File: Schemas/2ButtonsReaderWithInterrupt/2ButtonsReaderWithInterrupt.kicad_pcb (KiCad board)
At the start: 2 copper layers, 45.7 x 36.6 mm, 17 parts, among them J1 PWR, J2 Btn out, J3 Btn in, J4 Interrupt, U1 LM393

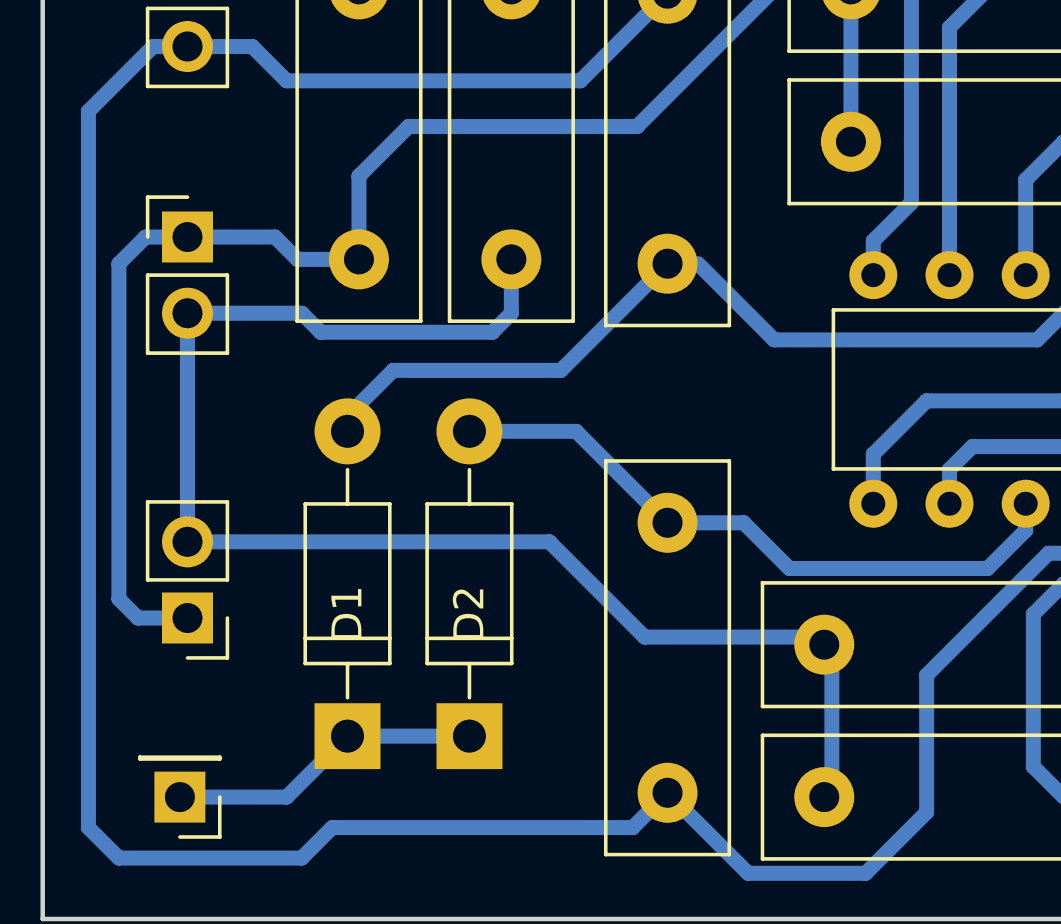
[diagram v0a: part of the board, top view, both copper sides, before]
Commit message: Add a pull down resistor
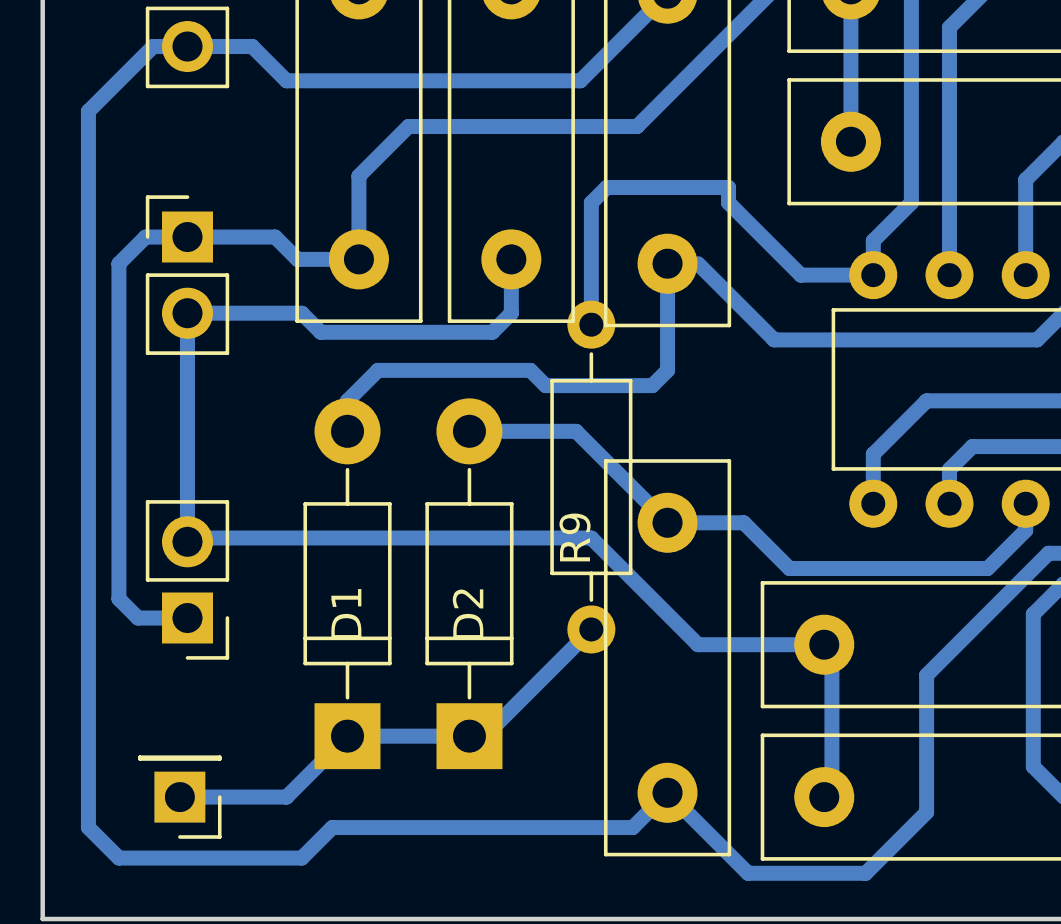
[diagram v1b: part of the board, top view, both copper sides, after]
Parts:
- added R9: R10k, Resistors_THT:R_Axial_DIN0207_L6.3mm_D2.5mm_P10.16mm_Horizontal, F.Cu at (118.9, 125.5)
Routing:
- net Net-(C2-Pad2): track 85.7 -> 100.9 mm
- net Net-(D1-Pad1): track 9.99 -> 15.5 mm
- net Net-(D1-Pad2): track 29.7 -> 33.0 mm
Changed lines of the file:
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@@
 (kicad_pcb (version 4) (host pcbnew 4.0.7-e2-6376~58~ubuntu16.04.1)
   (general
-    (links 28)
+    (links 30)
     (no_connects 0)
     (area 100.508999 108.636999 146.379001 145.363001)
     (thickness 1.6)
     (drawings 9)
-    (tracks 120)
+    (tracks 133)
     (zones 0)
-    (modules 17)
+    (modules 18)
     (nets 12)
   )
@@
     )
   )
+  (module Resistors_THT:R_Axial_DIN0207_L6.3mm_D2.5mm_P10.16mm_Horizontal (layer F.Cu)
+    (at 118.872 125.476 270)
+    (descr "Resistor, Axial_DIN0207 series, Axial, Horizontal, pin pitch=10.16mm, 0.25W = 1/4W, length*diameter=6.3*2.5mm^2, http://cdn-reichelt.de/documents/datenblatt/B400/1_4W%23YAG.pdf")
+    (tags "Resistor Axial_DIN0207 series Axial Horizontal pin pitch 10.16mm 0.25W = 1/4W length 6.3mm diameter 2.5mm")
+    (fp_text reference R9 (at 7.112 0.508 270) (layer F.SilkS)
+      (effects (font (size 1 1) (thickness 0.15)))
+    )
+    (fp_text value R10k (at 4.064 0.508 270) (layer F.Fab)
+      (effects (font (size 1 1) (thickness 0.15)))
+    )
+    (fp_line (start 1.93 -1.25) (end 1.93 1.25) (layer F.Fab) (width 0.1))
+    (fp_line (start 1.93 1.25) (end 8.23 1.25) (layer F.Fab) (width 0.1))
+    (fp_line (start 8.23 1.25) (end 8.23 -1.25) (layer F.Fab) (width 0.1))
+    (fp_line (start 8.23 -1.25) (end 1.93 -1.25) (layer F.Fab) (width 0.1))
+    (fp_line (start 0 0) (end 1.93 0) (layer F.Fab) (width 0.1))
+    (fp_line (start 10.16 0) (end 8.23 0) (layer F.Fab) (width 0.1))
+    (fp_line (start 1.87 -1.31) (end 1.87 1.31) (layer F.SilkS) (width 0.12))
+    (fp_line (start 1.87 1.31) (end 8.29 1.31) (layer F.SilkS) (width 0.12))
+    (fp_line (start 8.29 1.31) (end 8.29 -1.31) (layer F.SilkS) (width 0.12))
+    (fp_line (start 8.29 -1.31) (end 1.87 -1.31) (layer F.SilkS) (width 0.12))
+    (fp_line (start 0.98 0) (end 1.87 0) (layer F.SilkS) (width 0.12))
+    (fp_line (start 9.18 0) (end 8.29 0) (layer F.SilkS) (width 0.12))
+    (fp_line (start -1.05 -1.6) (end -1.05 1.6) (layer F.CrtYd) (width 0.05))
+    (fp_line (start -1.05 1.6) (end 11.25 1.6) (layer F.CrtYd) (width 0.05))
+    (fp_line (start 11.25 1.6) (end 11.25 -1.6) (layer F.CrtYd) (width 0.05))
+    (fp_line (start 11.25 -1.6) (end -1.05 -1.6) (layer F.CrtYd) (width 0.05))
+    (pad 1 thru_hole circle (at 0 0 270) (size 1.6 1.6) (drill 0.8) (layers *.Cu *.Mask)
+      (net 9 "Net-(C2-Pad2)"))
+    (pad 2 thru_hole oval (at 10.16 0 270) (size 1.6 1.6) (drill 0.8) (layers *.Cu *.Mask)
+      (net 3 "Net-(D1-Pad1)"))
+    (model ${KISYS3DMOD}/Resistors_THT.3dshapes/R_Axial_DIN0207_L6.3mm_D2.5mm_P10.16mm_Horizontal.wrl
+      (at (xyz 0 0 0))
+      (scale (xyz 0.393701 0.393701 0.393701))
+      (rotate (xyz 0 0 0))
+    )
+  )
   (gr_circle (center 142.748 122.936) (end 144.272 121.92) (layer Edge.Cuts) (width 0.15))
   (gr_text "1 2" (at 102.616 134.112 90) (layer Eco2.User)
@@
   (segment (start 139.192 140.716) (end 141.732 140.716) (width 0.5) (layer B.Cu) (net 2))
   (segment (start 138.684 141.224) (end 139.192 140.716) (width 0.5) (layer B.Cu) (net 2))
+  (segment (start 114.808 139.192) (end 115.316 139.192) (width 0.5) (layer B.Cu) (net 3) (status C00000))
+  (segment (start 115.316 139.192) (end 118.872 135.636) (width 0.5) (layer B.Cu) (net 3) (status C00000))
   (segment (start 110.744 139.192) (end 108.712 141.224) (width 0.5) (layer B.Cu) (net 3))
   (segment (start 108.712 141.224) (end 105.664 141.224) (width 0.5) (layer B.Cu) (net 3))
   (segment (start 114.808 139.192) (end 110.744 139.192) (width 0.5) (layer B.Cu) (net 3))
+  (segment (start 110.744 129.032) (end 110.744 128.016) (width 0.5) (layer B.Cu) (net 4))
+  (segment (start 110.744 128.016) (end 111.76 127) (width 0.5) (layer B.Cu) (net 4))
+  (segment (start 121.412 127) (end 121.412 123.444) (width 0.5) (layer B.Cu) (net 4))
+  (segment (start 120.904 127.508) (end 121.412 127) (width 0.5) (layer B.Cu) (net 4))
+  (segment (start 117.348 127.508) (end 120.904 127.508) (width 0.5) (layer B.Cu) (net 4))
+  (segment (start 116.84 127) (end 117.348 127.508) (width 0.5) (layer B.Cu) (net 4))
+  (segment (start 111.76 127) (end 116.84 127) (width 0.5) (layer B.Cu) (net 4))
   (segment (start 110.744 129.032) (end 110.744 128.524) (width 0.25) (layer B.Cu) (net 4))
-  (segment (start 110.744 128.524) (end 112.268 127) (width 0.5) (layer B.Cu) (net 4))
-  (segment (start 112.268 127) (end 117.856 127) (width 0.5) (layer B.Cu) (net 4))
-  (segment (start 117.856 127) (end 121.412 123.444) (width 0.5) (layer B.Cu) (net 4))
   (segment (start 121.412 123.444) (end 122.428 123.444) (width 0.25) (layer B.Cu) (net 4))
   (segment (start 133.731 125.984) (end 135.89 123.825) (width 0.5) (layer B.Cu) (net 4))
@@
   (segment (start 126.89 120.015) (end 127.525 119.38) (width 0.25) (layer B.Cu) (net 7))
   (segment (start 127.525 119.38) (end 127.525 114.3) (width 0.5) (layer B.Cu) (net 7))
+  (segment (start 126.636 136.144) (end 122.428 136.144) (width 0.5) (layer B.Cu) (net 8) (status 400000))
+  (segment (start 118.872 132.588) (end 105.537 132.588) (width 0.5) (layer B.Cu) (net 8) (status 800000))
+  (segment (start 122.428 136.144) (end 118.872 132.588) (width 0.5) (layer B.Cu) (net 8))
+  (segment (start 105.537 132.588) (end 105.41 132.715) (width 0.5) (layer B.Cu) (net 8) (status C00000))
   (segment (start 105.41 125.095) (end 109.22 125.095) (width 0.5) (layer B.Cu) (net 8))
   (segment (start 116.205 125.095) (end 116.205 123.3) (width 0.5) (layer B.Cu) (net 8))
@@
   (segment (start 109.855 125.73) (end 115.57 125.73) (width 0.5) (layer B.Cu) (net 8))
   (segment (start 109.22 125.095) (end 109.855 125.73) (width 0.5) (layer B.Cu) (net 8))
-  (segment (start 105.41 132.715) (end 117.475 132.715) (width 0.5) (layer B.Cu) (net 8))
-  (segment (start 120.65 135.89) (end 126.89 135.89) (width 0.5) (layer B.Cu) (net 8))
-  (segment (start 117.475 132.715) (end 120.65 135.89) (width 0.5) (layer B.Cu) (net 8))
   (segment (start 126.89 135.89) (end 126.89 140.97) (width 0.5) (layer B.Cu) (net 8))
   (segment (start 105.41 125.095) (end 105.41 132.715) (width 0.5) (layer B.Cu) (net 8))
+  (segment (start 128.27 123.825) (end 125.857 123.825) (width 0.5) (layer B.Cu) (net 9))
+  (segment (start 118.872 121.412) (end 118.872 125.476) (width 0.5) (layer B.Cu) (net 9))
+  (segment (start 119.38 120.904) (end 118.872 121.412) (width 0.5) (layer B.Cu) (net 9))
+  (segment (start 123.444 120.904) (end 119.38 120.904) (width 0.5) (layer B.Cu) (net 9))
+  (segment (start 123.444 121.412) (end 123.444 120.904) (width 0.5) (layer B.Cu) (net 9))
+  (segment (start 125.857 123.825) (end 123.444 121.412) (width 0.5) (layer B.Cu) (net 9))
   (segment (start 143.732 140.716) (end 143.732 135.604) (width 0.5) (layer B.Cu) (net 9))
   (segment (start 143.256 117.856) (end 143.256 114.332) (width 0.5) (layer B.Cu) (net 9))

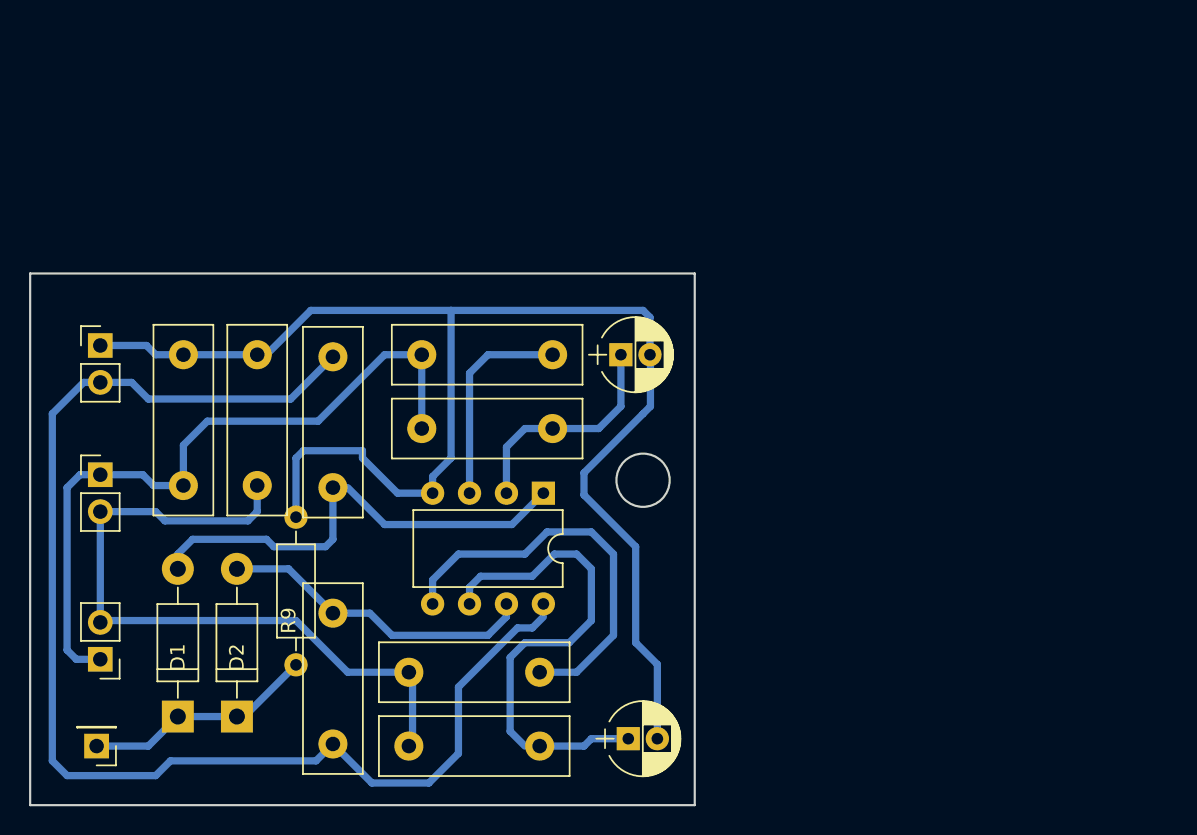
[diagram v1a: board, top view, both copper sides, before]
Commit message: Change 2ButtonsReaderWithInterrupt schema
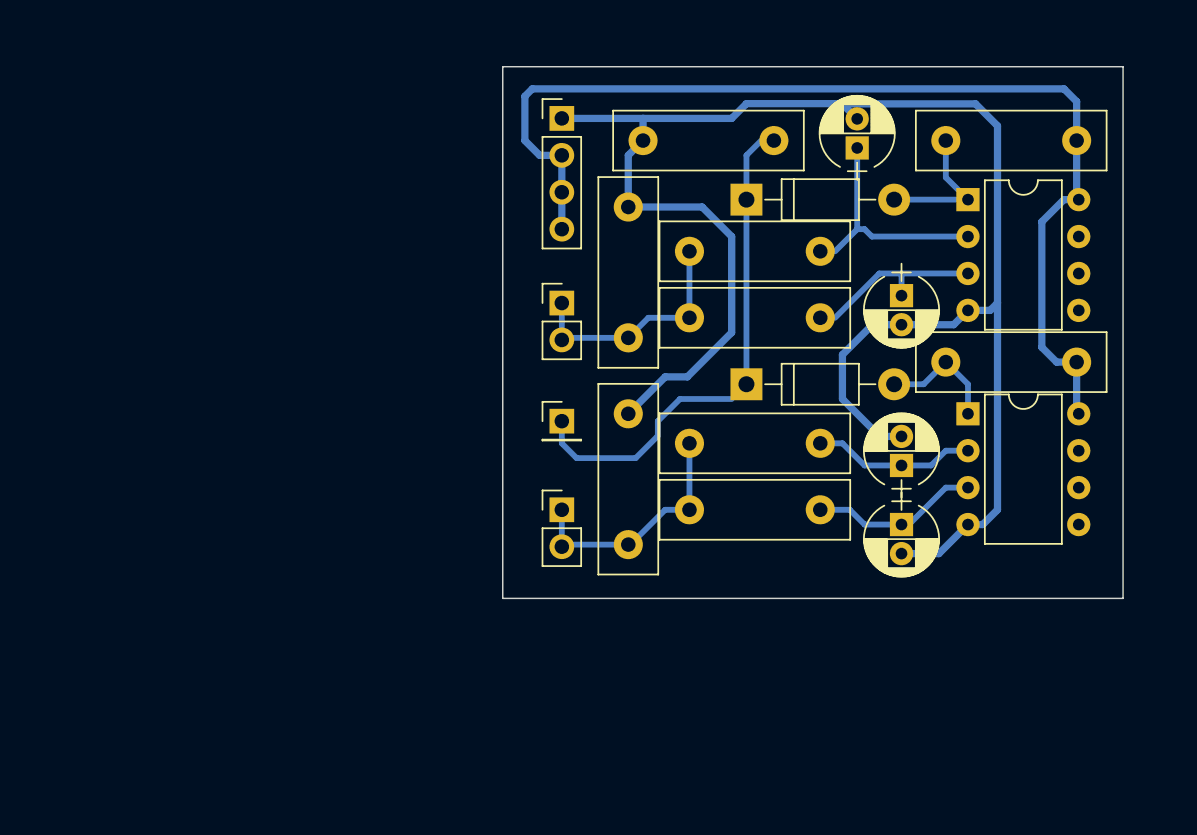
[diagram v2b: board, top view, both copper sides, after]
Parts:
- added C1: C2.2, Capacitors_THT:CP_Radial_D5.0mm_P2.00mm, F.Cu at (160.5, 110.2)
- added C3: C2.2, Capacitors_THT:CP_Radial_D5.0mm_P2.00mm, F.Cu at (160.5, 126.0)
- added U2: LM393, Housings_DIP:DIP-8_W7.62mm, F.Cu at (165.1, 118.4)
- C2, C4: value C2.2 -> C4.7
- J1: footprint Socket_Strips:Socket_Strip_Straight_1x02_Pitch2.54mm -> Socket_Strips:Socket_Strip_Straight_1x04_Pitch2.54mm
- J2: value Btn out -> Btn A
- J3: value Btn in -> Btn B
- R9: value R10k -> R100k; footprint Resistors_THT:R_Axial_DIN0207_L6.3mm_D2.5mm_P10.16mm_Horizontal -> Resistors_THT:R_Box_L13.0mm_W4.0mm_P9.00mm
- moved D1 52.9 mm to (149.9, 103.6), turned to 0 degrees
- moved R7 48.5 mm to (163.6, 99.6), turned to 0 degrees
- moved R8 45.6 mm to (163.6, 114.8), turned to 0 degrees
- moved D2 41.8 mm to (149.9, 116.3), turned to 0 degrees
- moved J2 40.1 mm to (137.2, 110.7), turned to 0 degrees
- moved J4 39.0 mm to (137.2, 118.9), turned to 0 degrees
- moved U1 35.5 mm to (165.1, 103.6), turned to 0 degrees
- moved J1 35.4 mm to (137.2, 98.0)
- moved R9 35.2 mm to (142.7, 99.6), turned to 0 degrees
- moved J3 31.8 mm to (137.2, 125.0)
- moved R2 30.9 mm to (141.7, 118.4)
- moved R6 28.4 mm to (154.9, 120.4)
- moved R1 27.5 mm to (141.7, 104.1)
- moved C4 26.6 mm to (160.5, 121.9), turned to 90 degrees
- moved R5 22.3 mm to (154.9, 125.0)
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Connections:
- J2 pad 2: Net-(J2-Pad2) -> Net-(J2-Pad1)
- J3 pad 1: Net-(J2-Pad1) -> Net-(J3-Pad1)
- J3 pad 2: Net-(J2-Pad2) -> Net-(J3-Pad1)
- R1 pad 2: Net-(J2-Pad2) -> Net-(J2-Pad1)
- R2 pad 2: Net-(J2-Pad1) -> Net-(J3-Pad1)
- R5 pad 1: Net-(R5-Pad1) -> Net-(C3-Pad1)
- R5 pad 2: Net-(J2-Pad2) -> Net-(J3-Pad1)
- R6 pad 2: Net-(J2-Pad2) -> Net-(J3-Pad1)
- U1 pad 5: Net-(R5-Pad1) -> (no net)
- U1 pad 6: Net-(C4-Pad1) -> (no net)
- U1 pad 7: Net-(D2-Pad2) -> (no net)
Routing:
- net Net-(J2-Pad2): track 48.6 -> 0.00 mm
- net Net-(J2-Pad1): track 50.1 -> 17.2 mm
- net Net-(R5-Pad1): track 27.8 -> 0.00 mm
- net Net-(C4-Pad1): track 34.9 -> 11.2 mm
- net Net-(D1-Pad2): track 33.0 -> 9.78 mm
- net Net-(D1-Pad1): track 15.5 -> 36.1 mm
- net Net-(C1-Pad2): track 100.9 -> 118.1 mm
- net Net-(J3-Pad1): track 0.00 -> 16.9 mm
- net Net-(J1-Pad2): track 90.3 -> 74.7 mm
- net Net-(D2-Pad2): track 21.9 -> 8.37 mm
- net Net-(C3-Pad1): track 0.00 -> 11.6 mm
- net Net-(C1-Pad1): track 14.5 -> 12.9 mm
- net Net-(C2-Pad1): track 15.8 -> 16.6 mm
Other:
- board size 45.7 x 36.6 mm -> 42.7 x 36.6 mm
- net class Default: trace_width 0.5 -> 0.4
- net class PWR added: clearance 0.2, trace_width 0.5, via_dia 0.6, via_drill 0.4
- rule pad_to_mask_clearance: 0.2 -> 0
- rule trace_min: 0.2 -> 0.4
- board text added: "2 chnl int"
- board text removed: "1 2"
- board text removed: "2 1"

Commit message: Update 2ButtonsReaderWithInterrupt, remove layout/
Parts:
- moved D1 2.09 mm to (147.8, 103.1)
- moved J3 2.09 mm to (135.1, 124.5)
- moved R2 2.09 mm to (139.7, 117.9)
- moved R3 2.09 mm to (152.9, 111.3)
- moved R5 2.09 mm to (152.9, 124.5)
- moved D2 2.09 mm to (147.8, 115.8)
- moved J1 2.09 mm to (135.1, 97.5)
- moved J2 2.09 mm to (135.1, 110.2)
- moved J4 2.09 mm to (135.1, 118.4)
- moved R1 2.09 mm to (139.7, 103.6)
- moved R4 2.09 mm to (152.9, 106.7)
- moved R6 2.09 mm to (152.9, 119.9)
- moved C1 2.09 mm to (158.5, 109.7)
- moved R8 2.09 mm to (161.5, 114.3)
- moved U1 2.09 mm to (163.1, 103.1)
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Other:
- board size 42.7 x 36.6 mm -> 48.8 x 41.1 mm
